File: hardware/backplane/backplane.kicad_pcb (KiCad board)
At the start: 4 copper layers, 192 x 29.5 mm, 31 parts, among them J1 Mgmt_Module, J10 Bus_PCI_Express_x1, J11 UPS_UART, J2 PWR, J3 Bus_PCI_Express_x1, J4 Bus_PCI_Express_x1, J5 Bus_PCI_Express_x1, J6 Bus_PCI_Express_x1, J7 Bus_PCI_Express_x1, J8 Bus_PCI_Express_x1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

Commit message: fix: add decoupling caps to i2c and swd switches
fix: add pullup resistor to i2c switch reset pin
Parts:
- removed M4: FAN4, Connector:FanPinHeader_1x03_P2.54mm_Vertical
- added C5: 10uF, Capacitor_SMD:C_0805_2012Metric, F.Cu at (60.7, 63.8)
- added C6: 10uF, Capacitor_SMD:C_0805_2012Metric, F.Cu at (62.8, 63.8)
- added R4: 10K, Resistor_SMD:R_0603_1608Metric, F.Cu at (75.1, 62.8)
- moved M1 137.8 mm to (194.0, 67.2)
- moved M2 6.90 mm to (194.0, 60.3)
- moved M3 6.90 mm to (194.0, 53.4)
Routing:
- net VDD: track 43.7 -> 57.0 mm
- net I2C_RESET: track 28.7 -> 31.8 mm
- net SCL: track 183.5 -> 181.8 mm
- net SWD: track 30.2 -> 31.5 mm
- net GND: vias 12 -> 11

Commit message: chore: add open hardware logo
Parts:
- added REF**: OSHW-Logo2_7.3x6mm_SilkScreen, Symbol:OSHW-Logo2_7.3x6mm_SilkScreen, F.Cu at (68.1, 76.3)
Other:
- board text removed: "5V FAN"

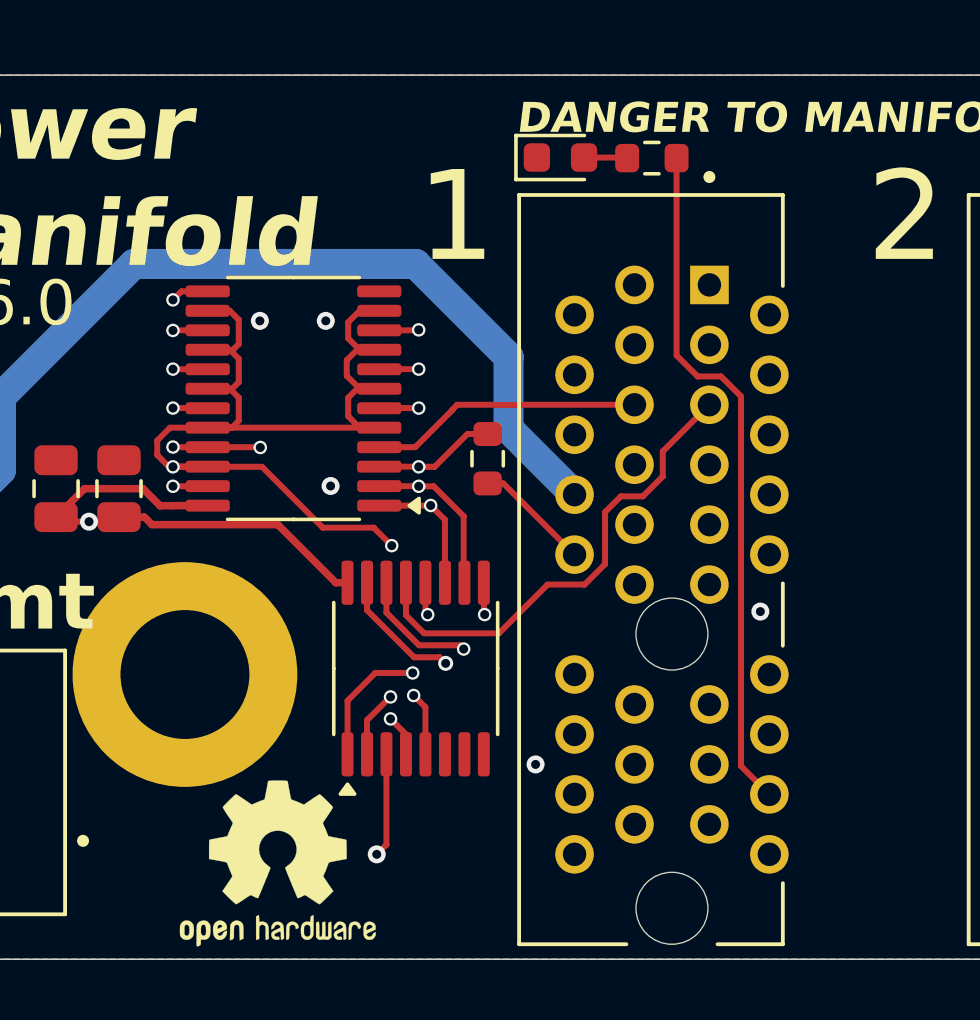
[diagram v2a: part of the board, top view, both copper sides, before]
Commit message: feat: give vin 8 pins
fix: correct i2c pin mismatch
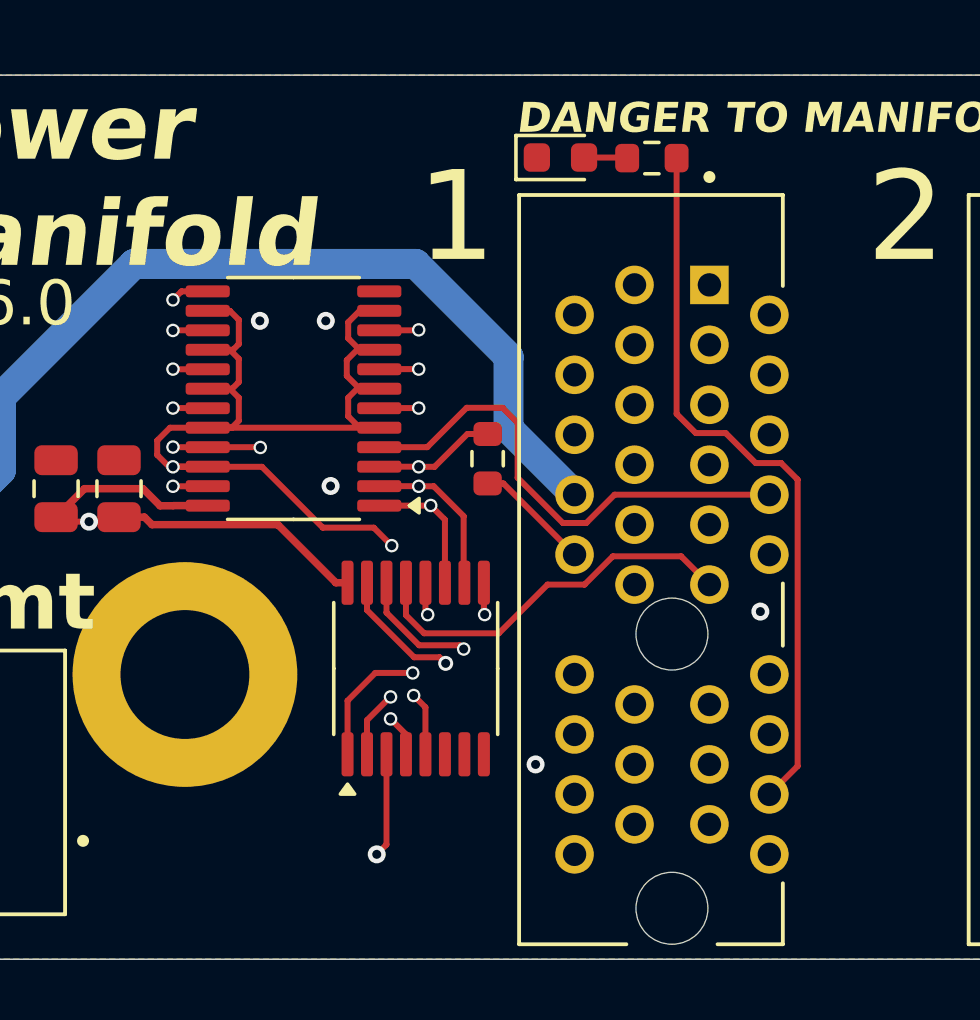
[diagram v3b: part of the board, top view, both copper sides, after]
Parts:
- removed REF**: OSHW-Logo2_7.3x6mm_SilkScreen, Symbol:OSHW-Logo2_7.3x6mm_SilkScreen
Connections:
- J10 pad A11: unconnected-(J10-~{PERST}-PadA11) -> SWD8
- J10 pad A5: SWD8 -> GND
- J10 pad A6: unconnected-(J10-JTAG3-PadA6) -> GND
- J10 pad A8: unconnected-(J10-JTAG5-PadA8) -> SDA8
- J10 pad B5: SDA8 -> VIN
- J10 pad B6: unconnected-(J10-SMDAT-PadB6) -> VIN
- J3 pad A11: unconnected-(J3-~{PERST}-PadA11) -> SWD1
- J3 pad A5: SWD1 -> GND
- J3 pad A6: unconnected-(J3-JTAG3-PadA6) -> GND
- J3 pad A8: unconnected-(J3-JTAG5-PadA8) -> SDA1
- J3 pad B5: SDA1 -> VIN
- J3 pad B6: unconnected-(J3-SMDAT-PadB6) -> VIN
- J4 pad A11: unconnected-(J4-~{PERST}-PadA11) -> SWD5
- J4 pad A5: SWD5 -> GND
- J4 pad A6: unconnected-(J4-JTAG3-PadA6) -> GND
- J4 pad A8: unconnected-(J4-JTAG5-PadA8) -> SDA5
- J4 pad B5: SDA5 -> VIN
- J4 pad B6: unconnected-(J4-SMDAT-PadB6) -> VIN
- J5 pad A11: unconnected-(J5-~{PERST}-PadA11) -> SWD2
- J5 pad A5: SWD2 -> GND
- J5 pad A6: unconnected-(J5-JTAG3-PadA6) -> GND
- J5 pad A8: unconnected-(J5-JTAG5-PadA8) -> SDA2
- J5 pad B5: SDA2 -> VIN
- J5 pad B6: unconnected-(J5-SMDAT-PadB6) -> VIN
- J6 pad A11: unconnected-(J6-~{PERST}-PadA11) -> SWD6
- J6 pad A5: SWD6 -> GND
- J6 pad A6: unconnected-(J6-JTAG3-PadA6) -> GND
- J6 pad A8: unconnected-(J6-JTAG5-PadA8) -> SDA6
- J6 pad B5: SDA6 -> VIN
- J6 pad B6: unconnected-(J6-SMDAT-PadB6) -> VIN
- J7 pad A11: unconnected-(J7-~{PERST}-PadA11) -> SWD3
- J7 pad A5: SWD3 -> GND
- J7 pad A6: unconnected-(J7-JTAG3-PadA6) -> GND
- J7 pad A8: unconnected-(J7-JTAG5-PadA8) -> SDA3
- J7 pad B5: SDA3 -> VIN
- J7 pad B6: unconnected-(J7-SMDAT-PadB6) -> VIN
- J8 pad A11: unconnected-(J8-~{PERST}-PadA11) -> SWD7
- J8 pad A5: SWD7 -> GND
- J8 pad A6: unconnected-(J8-JTAG3-PadA6) -> GND
- J8 pad A8: unconnected-(J8-JTAG5-PadA8) -> SDA7
- J8 pad B5: SDA7 -> VIN
- J8 pad B6: unconnected-(J8-SMDAT-PadB6) -> VIN
- J9 pad A11: unconnected-(J9-~{PERST}-PadA11) -> SWD4
- J9 pad A5: SWD4 -> GND
- J9 pad A6: unconnected-(J9-JTAG3-PadA6) -> GND
- J9 pad A8: unconnected-(J9-JTAG5-PadA8) -> SDA4
- J9 pad B5: SDA4 -> VIN
- J9 pad B6: unconnected-(J9-SMDAT-PadB6) -> VIN
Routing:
- net +5V: track 75.4 -> 87.4 mm
- net SDA8: track 132.8 -> 144.3 mm
- net SDA7: track 115.5 -> 126.8 mm
- net SDA5: track 81.0 -> 92.1 mm
- net SDA4: track 57.9 -> 69.0 mm
- net SDA2: track 29.2 -> 40.3 mm
- net SDA6: track 98.2 -> 109.2 mm
- net SDA3: track 43.5 -> 54.5 mm
- net SDA1: track 9.11 -> 16.6 mm
- net SWD8: track 137.1 -> 143.1 mm
- net SWD6: track 105.5 -> 111.5 mm
- net SWD4: track 69.7 -> 75.7 mm
- net SWD3: track 58.6 -> 64.6 mm
- net SWD2: track 42.0 -> 48.0 mm
- net SWD7: track 121.3 -> 127.3 mm
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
